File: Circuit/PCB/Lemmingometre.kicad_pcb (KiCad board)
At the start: 2 copper layers, 30.6 x 77.6 mm, 16 parts

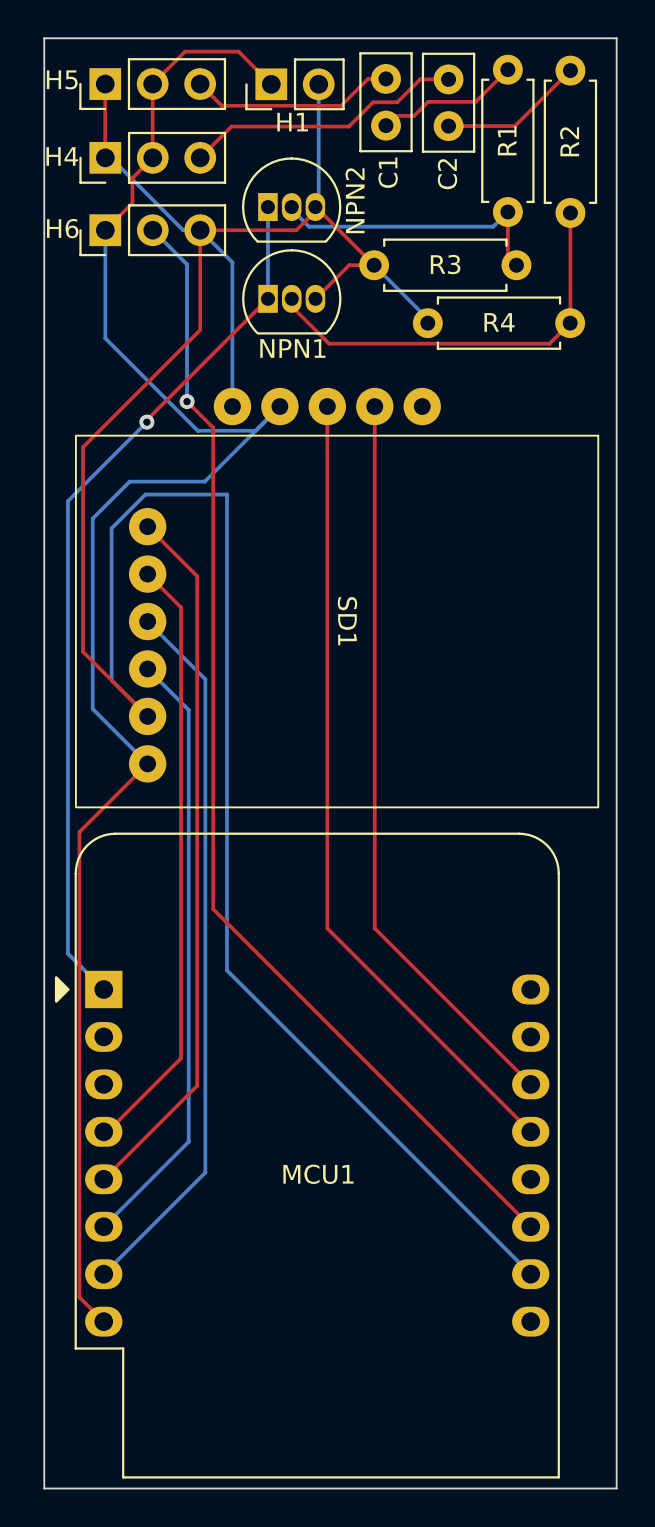
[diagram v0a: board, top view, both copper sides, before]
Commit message: changed schematic and pcb
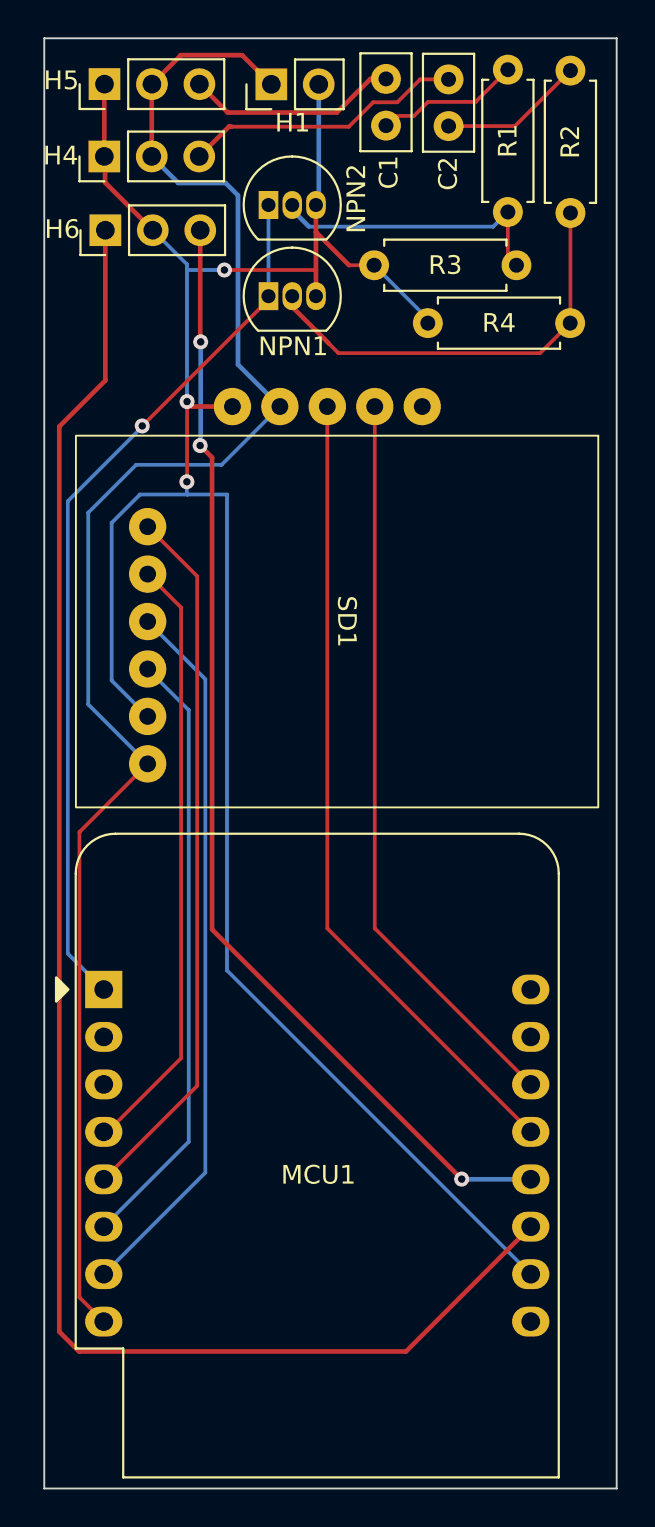
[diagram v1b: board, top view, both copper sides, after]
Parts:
- R3, R4: value 5k -> 100k
- moved NPN1 0.15 mm to (155.9, 57.0)
- moved NPN2 0.11 mm to (155.9, 52.1)
- moved H4 0.09 mm to (147.1, 49.5)
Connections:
- H6 pad 1: Net-(H1-Pin_1) -> Net-(H6-Pin_1)
- H6 pad 2: Net-(H6-Pin_2) -> Net-(H1-Pin_2)
- H6 pad 3: Net-(H1-Pin_2) -> Net-(H6-Pin_3)
- MCU1 pad 11: Net-(H6-Pin_2) -> Net-(H6-Pin_1)
- MCU1 pad 12: unconnected-(MCU1-D3-Pad12) -> Net-(H6-Pin_3)
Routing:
- net Net-(H6-Pin_1): track 0.00 -> 88.9 mm
- net Net-(H6-Pin_2): track 61.7 -> 0.00 mm, vias 1 -> 0
- net Net-(H6-Pin_3): track 0.00 -> 60.3 mm, vias 0 -> 3
- net Net-(H1-Pin_2): track 143.2 -> 119.1 mm, vias 0 -> 3
- net Net-(H1-Pin_1): track 93.2 -> 88.6 mm
- net Net-(NPN1-B): track 22.5 -> 23.1 mm

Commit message: Changed from IR to PIR sensor
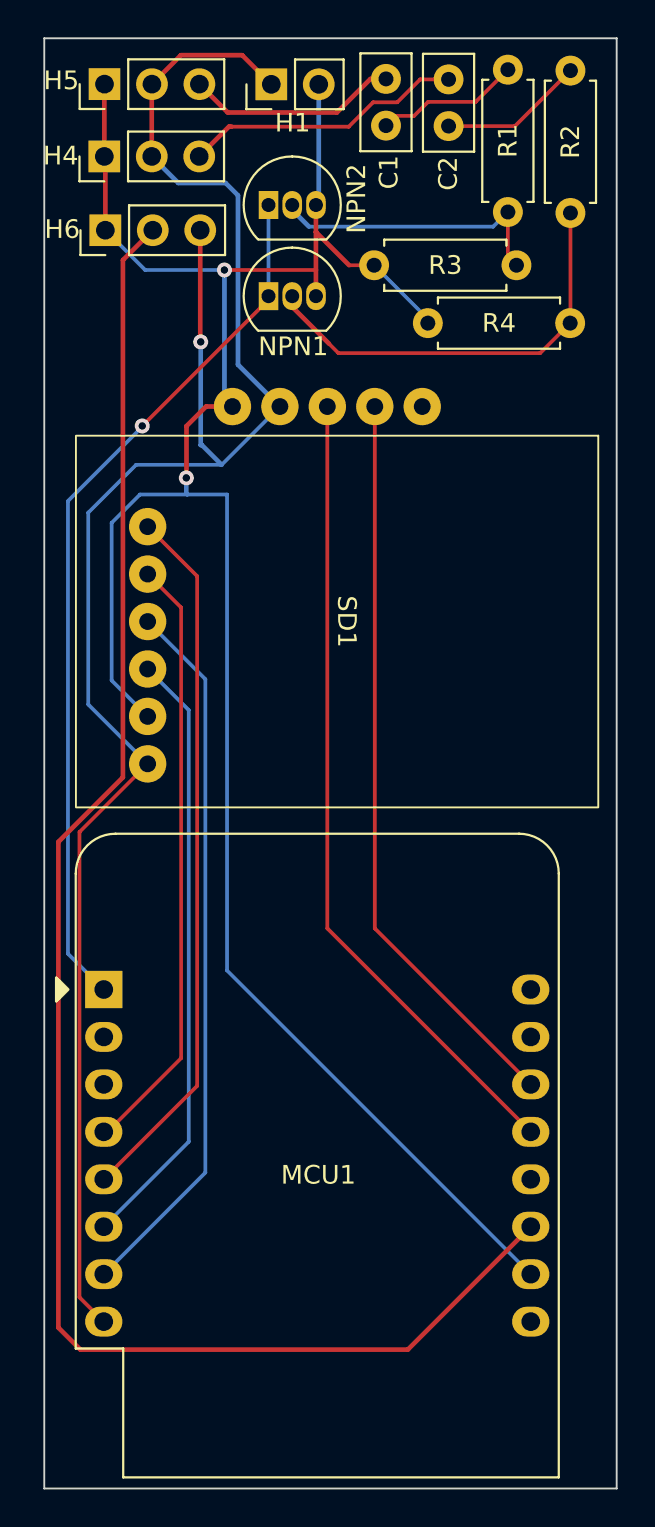
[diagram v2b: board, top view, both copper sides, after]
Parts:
- H6: value Conn_IR -> Conn_PIR3
- R1, R2: value R -> 1k
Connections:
- H6 pad 1: Net-(H6-Pin_1) -> Net-(H1-Pin_2)
- H6 pad 2: Net-(H1-Pin_2) -> Net-(H6-Pin_2)
- H6 pad 3: Net-(H6-Pin_3) -> Net-(H1-Pin_1)
- MCU1 pad 11: Net-(H6-Pin_1) -> Net-(H6-Pin_2)
- MCU1 pad 12: Net-(H6-Pin_3) -> unconnected-(MCU1-D3-Pad12)
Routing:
- net Net-(H6-Pin_2): track 0.00 -> 90.3 mm
- net Net-(H6-Pin_1): track 88.9 -> 0.00 mm
- net Net-(H6-Pin_3): track 60.3 -> 0.00 mm, vias 3 -> 0
- net Net-(H1-Pin_1): track 88.6 -> 101.6 mm, vias 0 -> 1
- net Net-(H1-Pin_2): track 119.1 -> 120.1 mm, vias 3 -> 2

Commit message: spaced pcb routes
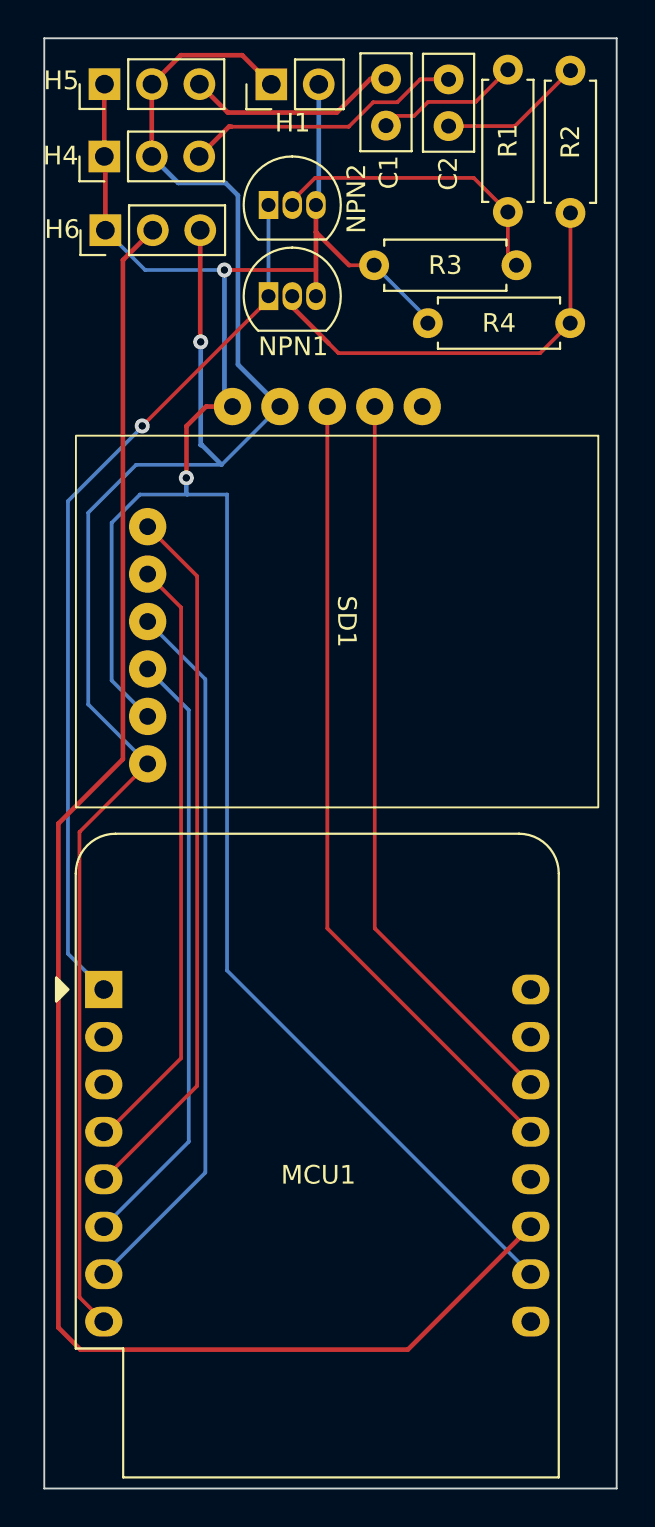
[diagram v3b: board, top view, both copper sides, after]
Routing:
- net Net-(NPN2-B): track 15.7 -> 16.5 mm
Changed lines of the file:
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@@
   (segment (start 157.18 57.03) (end 157.18 57.605) (width 0.25) (layer "F.Cu") (net 3))
   (segment (start 170.455 60.08) (end 159.655 60.08) (width 0.2) (layer "F.Cu") (net 3))
+  (segment (start 157.18 51.925) (end 157.18 52.15) (width 0.2) (layer "F.Cu") (net 4))
+  (segment (start 166.9 50.7) (end 158.405 50.7) (width 0.2) (layer "F.Cu") (net 4))
   (segment (start 168.725 52.525) (end 168.725 54.915) (width 0.2) (layer "F.Cu") (net 4))
+  (segment (start 158.405 50.7) (end 157.18 51.925) (width 0.2) (layer "F.Cu") (net 4))
+  (segment (start 168.725 52.525) (end 166.9 50.7) (width 0.2) (layer "F.Cu") (net 4))
   (segment (start 168.725 54.915) (end 169.185 55.375) (width 0.2) (layer "F.Cu") (net 4))
   (segment (start 157.18 52.15) (end 157.18 52.411726) (width 0.25) (layer "B.Cu") (net 4))
-  (segment (start 158.078274 53.31) (end 167.94 53.31) (width 0.2) (layer "B.Cu") (net 4))
-  (segment (start 167.94 53.31) (end 168.725 52.525) (width 0.2) (layer "B.Cu") (net 4))
   (segment (start 157.15 52.26) (end 157.15 52.381726) (width 0.2) (layer "B.Cu") (net 4))
-  (segment (start 157.18 52.411726) (end 158.078274 53.31) (width 0.25) (layer "B.Cu") (net 4))
   (segment (start 159.57 47.2) (end 161.37 45.4) (width 0.25) (layer "F.Cu") (net 5))
   (segment (start 152.21 45.68) (end 153.73 47.2) (width 0.25) (layer "F.Cu") (net 5))
@@
   (segment (start 161.6 62.94) (end 161.6 90.88) (width 0.2) (layer "F.Cu") (net 20))
   (segment (start 161.6 90.88) (end 169.95 99.23) (width 0.2) (layer "F.Cu") (net 20))
+  (segment (start 163.37 113.43) (end 169.95 106.85) (width 0.25) (layer "F.Cu") (net 22))
+  (segment (start 148.115 55.1) (end 148.115 81.815) (width 0.25) (layer "F.Cu") (net 22))
+  (segment (start 149.715 53.5) (end 148.115 55.1) (width 0.25) (layer "F.Cu") (net 22))
   (segment (start 170.12604 107.275) (end 170.25052 107.15052) (width 0.25) (layer "F.Cu") (net 22))
   (segment (start 169.385 107.275) (end 170.12604 107.275) (width 0.25) (layer "F.Cu") (net 22))
-  (segment (start 149.715 53.5) (end 148.115 55.1) (width 0.25) (layer "F.Cu") (net 22))
-  (segment (start 148.115 82.79396) (end 144.66 86.24896) (width 0.25) (layer "F.Cu") (net 22))
-  (segment (start 148.115 55.1) (end 148.115 82.79396) (width 0.25) (layer "F.Cu") (net 22))
-  (segment (start 163.37 113.43) (end 169.95 106.85) (width 0.25) (layer "F.Cu") (net 22))
-  (segment (start 144.66 86.24896) (end 144.66 112.25) (width 0.25) (layer "F.Cu") (net 22))
   (segment (start 144.66 112.25) (end 145.84 113.43) (width 0.25) (layer "F.Cu") (net 22))
+  (segment (start 144.66 85.27) (end 144.66 112.25) (width 0.25) (layer "F.Cu") (net 22))
   (segment (start 145.84 113.43) (end 163.37 113.43) (width 0.25) (layer "F.Cu") (net 22))
+  (segment (start 148.115 81.815) (end 144.66 85.27) (width 0.25) (layer "F.Cu") (net 22))
 )
